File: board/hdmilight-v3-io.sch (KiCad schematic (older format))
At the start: 51 parts, among them J10 Conn_01x08, J11 Screw_Terminal_01x02, J12 Conn_01x02_Male, J13 Conn_01x16_Male, J4 Conn_01x08, J5 Conn_01x08, J6 Conn_01x08, J7 Conn_02x05_Odd_Even, J8 6P6C, J9 6P6C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

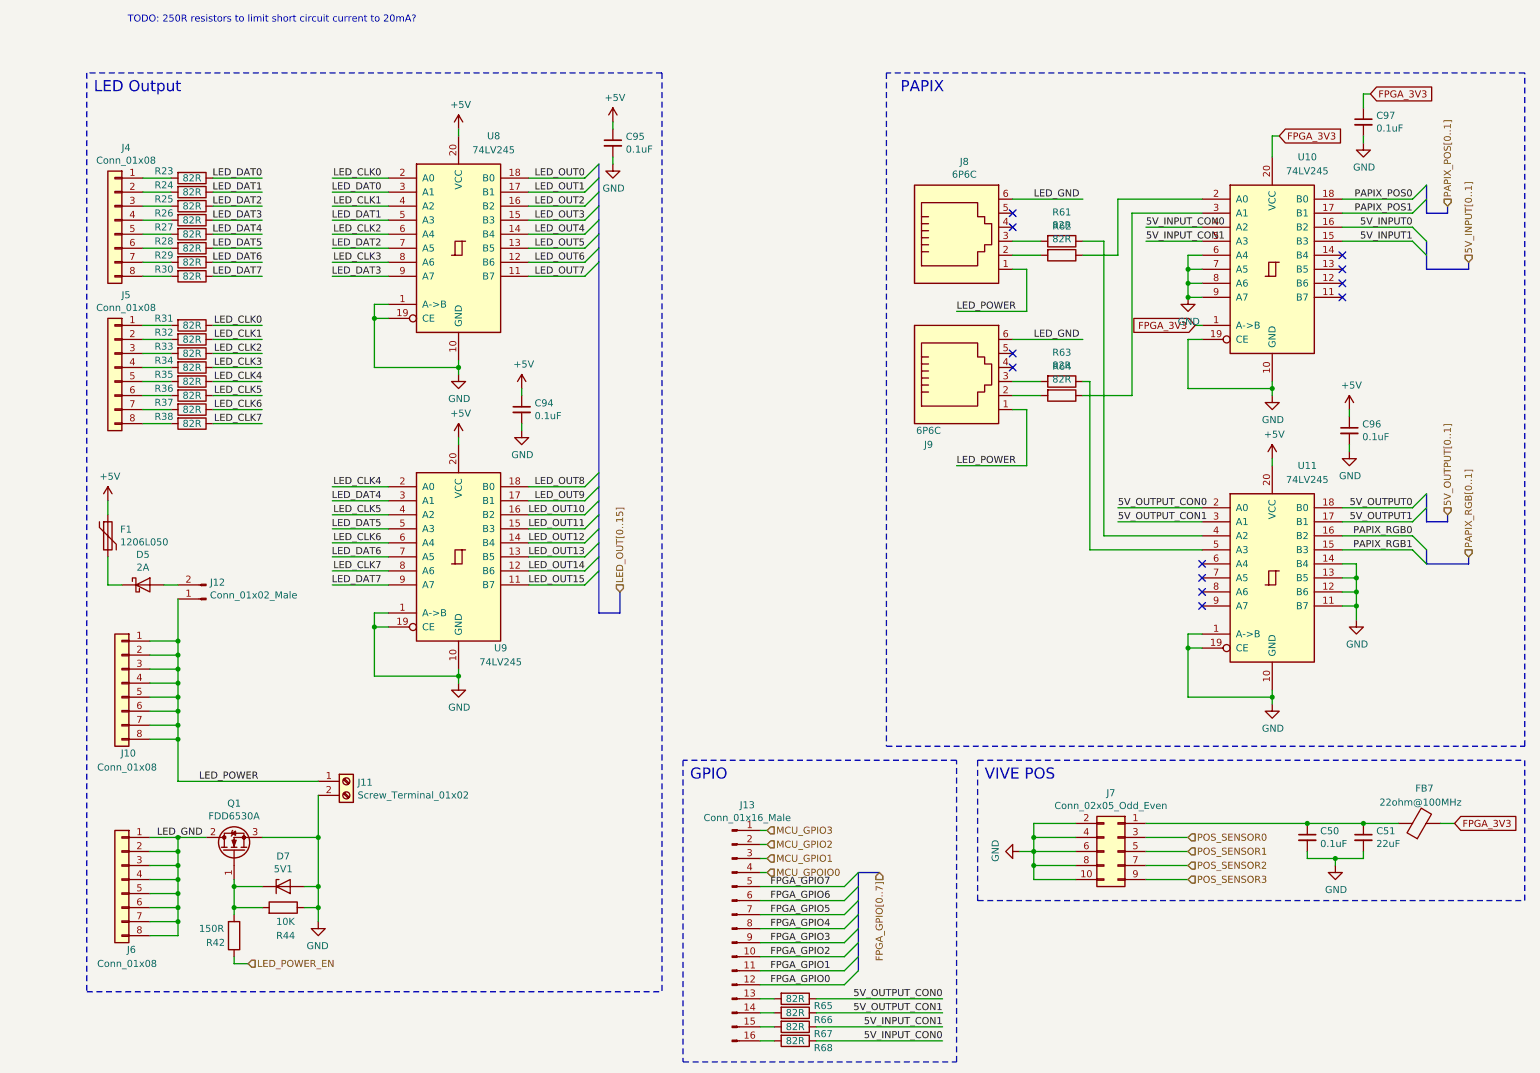
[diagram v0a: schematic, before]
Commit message: Fixed bugs in v3.0 board:
 * Changed FPGA GPIO to 2 row with ground to make it compatible with logic analyser plug for debugging
 * Move position sensor from PB4 to PB5
 * Connect voltage regulator center pad to ground pins
 * Add SPI CS line between FPGA and MCU
 * Move HDMI hotplug LED back from board edge
 * Move HDMI ESD chip closer to connector
 * Swap serial rx/tx
 * Fix FPGA EEPROM footprint
 * Fix reset button footprint
 * Connect ADV I2C to MCU
 * Fix missing ground to hotplug power off circuit
 * Move LED power connector to back of board
 * Move standby button to front of board
 * Only use HDMI 5v for hotplug detect
 * Change LED power switching to high side to stop it grounding back through the data line
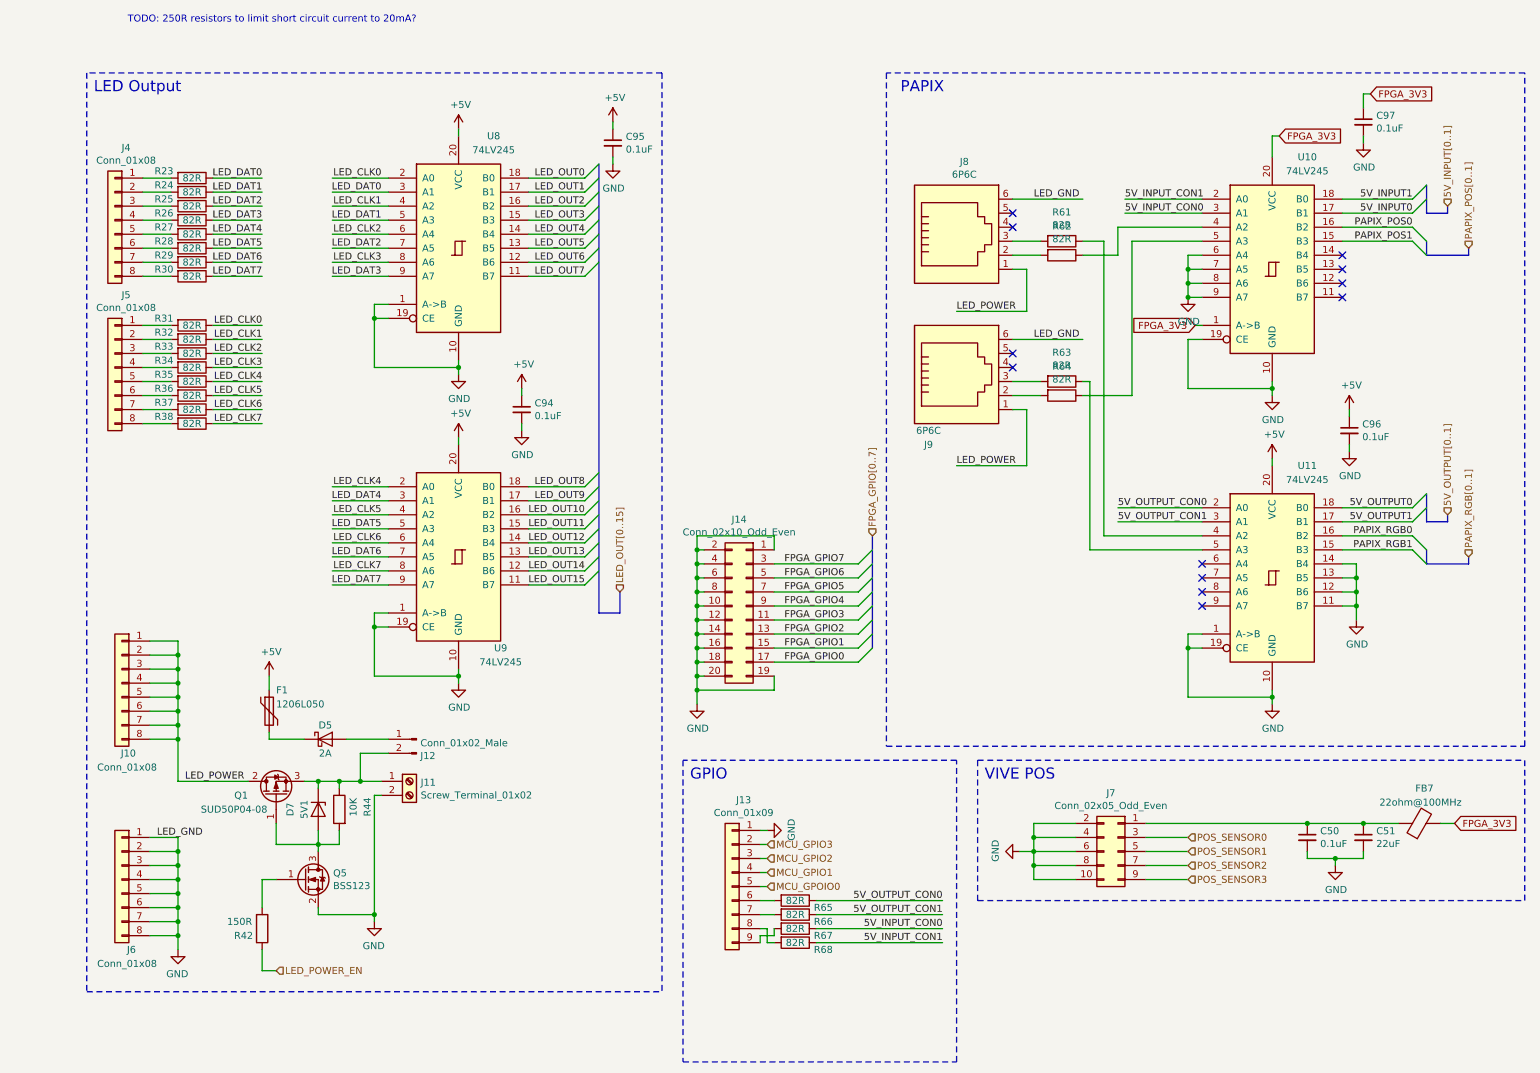
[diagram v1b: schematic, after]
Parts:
- removed J13: Conn_01x16_Male, Connector_PinHeader_2.54mm:PinHeader_1x16_P2.54mm_Horizontal, symbol Connector:Conn_01x16_Male
- removed Q1: FDD6530A, Package_TO_SOT_SMD:TO-252-2, symbol Transistor_FET:QM6006D
- added J13: Conn_01x09, Connector_PinSocket_2.54mm:PinSocket_1x09_P2.54mm_Vertical, symbol Connector_Generic:Conn_01x09
- added J14: Conn_02x10_Odd_Even, Connector_PinHeader_2.54mm:PinHeader_2x10_P2.54mm_Horizontal, symbol Connector_Generic:Conn_02x10_Odd_Even
- added Q1: SUD50P04-08, Package_TO_SOT_SMD:TO-252-2, symbol Transistor_FET:SUD50P04-08
- added Q5: BSS123, Package_TO_SOT_SMD:SOT-23, symbol Transistor_FET:BSS123
- J12: footprint Connector_PinHeader_2.54mm:PinHeader_1x02_P2.54mm_Horizontal -> Connector_PinHeader_2.54mm:PinHeader_1x02_P2.54mm_Vertical
- J7: footprint Connector_PinHeader_2.54mm:PinHeader_2x05_P2.54mm_Vertical -> Connector_IDC:IDC-Header_2x05_P2.54mm_Horizontal
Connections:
- wire segments 251 -> 290
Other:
- moved on the sheet: D5, D7, F1, J11, J12, R42, R44, R65, R66, R67, R68

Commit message: Fix level shifter part number 74LV245 -> 74LVC245
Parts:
- U10, U11, U8, U9: value 74LV245 -> 74LVC245
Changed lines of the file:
@@
 P 3300 1900
 F 0 "U8" H 3550 2700 50  0000 C CNN
-F 1 "74LV245" H 3550 2600 50  0000 C CNN
+F 1 "74LVC245" H 3550 2600 50  0000 C CNN
 F 2 "Package_SO:TSSOP-20_4.4x6.5mm_P0.65mm" H 3300 1900 50  0001 C CNN
 F 3 "" H 3300 1900 50  0001 C CNN
@@
 P 3300 4100
 F 0 "U9" H 3600 3450 50  0000 C CNN
-F 1 "74LV245" H 3600 3350 50  0000 C CNN
+F 1 "74LVC245" H 3600 3350 50  0000 C CNN
 F 2 "Package_SO:TSSOP-20_4.4x6.5mm_P0.65mm" H 3300 4100 50  0001 C CNN
 F 3 "" H 3300 4100 50  0001 C CNN
@@
 P 9100 2050
 F 0 "U10" H 9350 2850 50  0000 C CNN
-F 1 "74LV245" H 9350 2750 50  0000 C CNN
+F 1 "74LVC245" H 9350 2750 50  0000 C CNN
 F 2 "Package_SO:TSSOP-20_4.4x6.5mm_P0.65mm" H 9100 2050 50  0001 C CNN
 F 3 "" H 9100 2050 50  0001 C CNN
@@
 P 9100 4250
 F 0 "U11" H 9350 5050 50  0000 C CNN
-F 1 "74LV245" H 9350 4950 50  0000 C CNN
+F 1 "74LVC245" H 9350 4950 50  0000 C CNN
 F 2 "Package_SO:TSSOP-20_4.4x6.5mm_P0.65mm" H 9100 4250 50  0001 C CNN
 F 3 "" H 9100 4250 50  0001 C CNN

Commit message: BOM updates
 * Don't need EEPROM for FTDI
 * Change LED power switching transistor to the one I actually used
 * Sync CSV and interactive BOM files
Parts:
- Q1: value SUD50P04-08 -> IPD90P03P4L04
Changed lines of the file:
@@
 P 2000 5800
 F 0 "Q1" V 2000 6050 50  0000 C CNN
-F 1 "SUD50P04-08" V 1900 6100 50  0000 C CNN
+F 1 "IPD90P03P4L04" V 1900 6100 50  0000 C CNN
 F 2 "Package_TO_SOT_SMD:TO-252-2" H 2195 5725 50  0001 L CIN
 F 3 "https://www.vishay.com/docs/65594/sud50p04-08.pdf" H 2000 5800 50  0001 C CNN
